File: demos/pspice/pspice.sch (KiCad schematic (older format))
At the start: 20 parts, among them Q1 Q2N2222, Q2 Q2N2222, Q3 Q2N2222

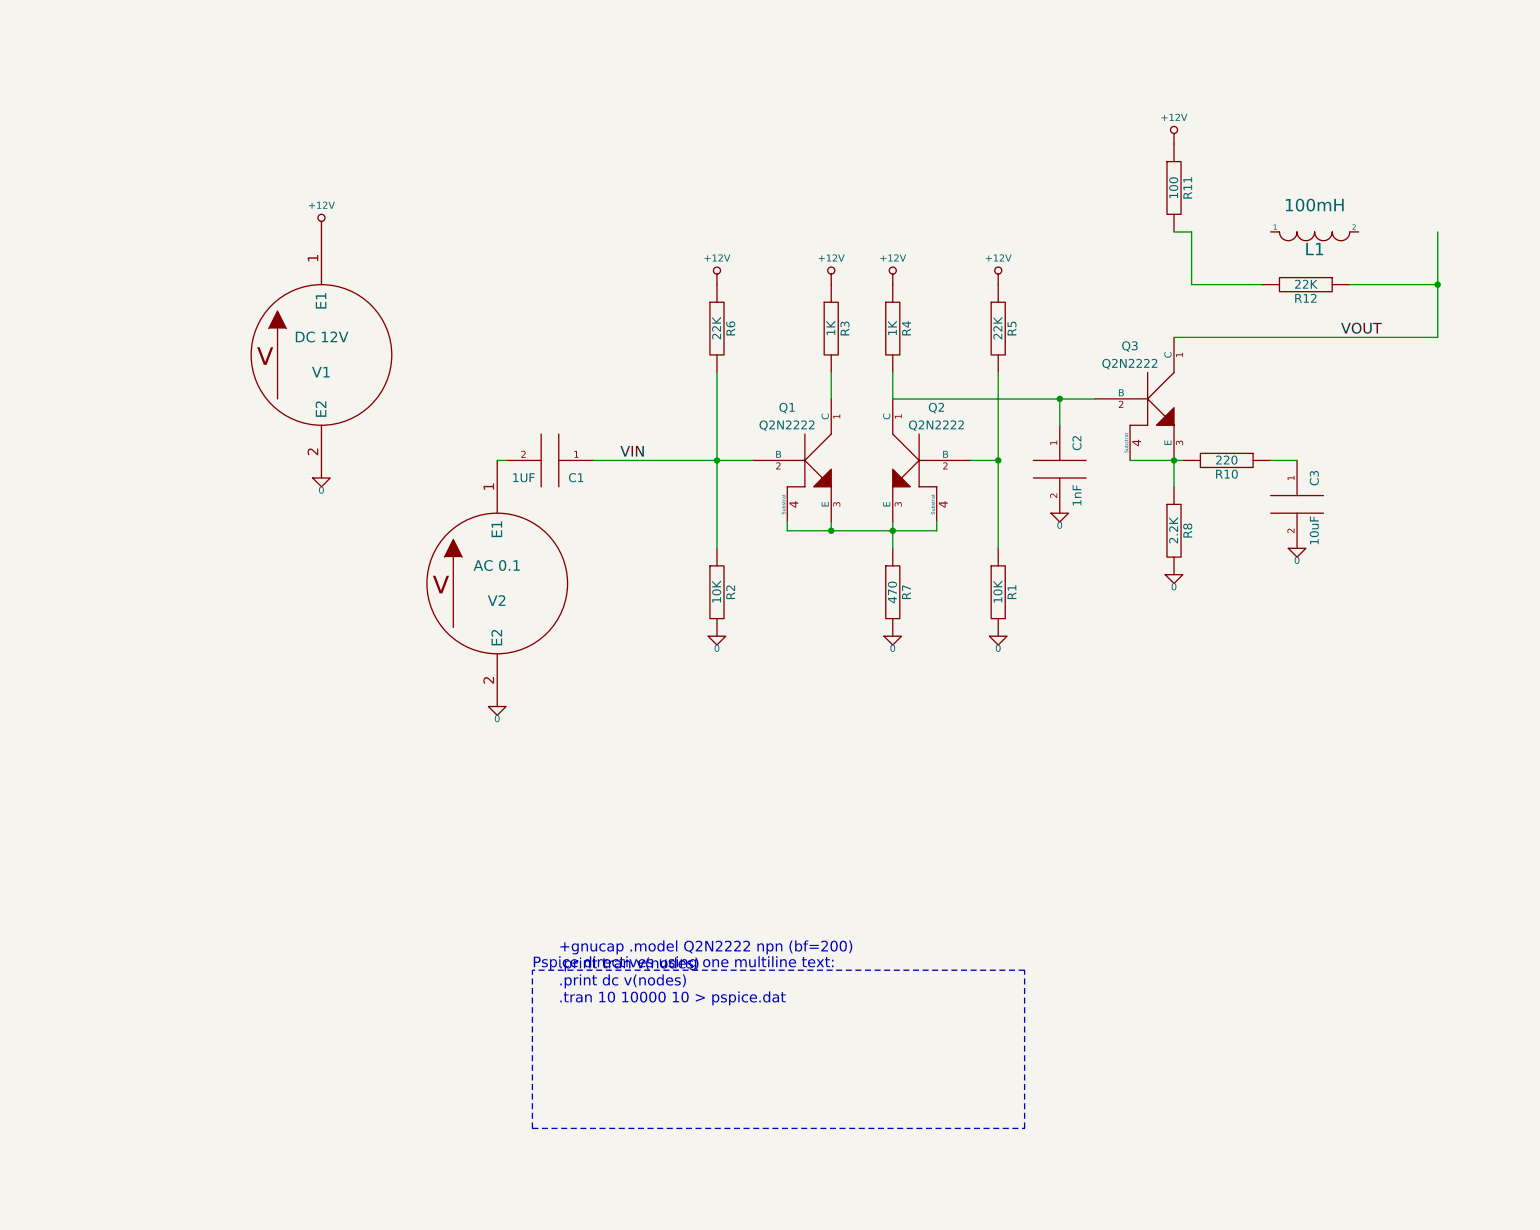
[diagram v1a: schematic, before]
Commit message: Update demos. Fix  pspice netlist issues when using ( and ) in net names ( parenthesis are replaced by underscore) .
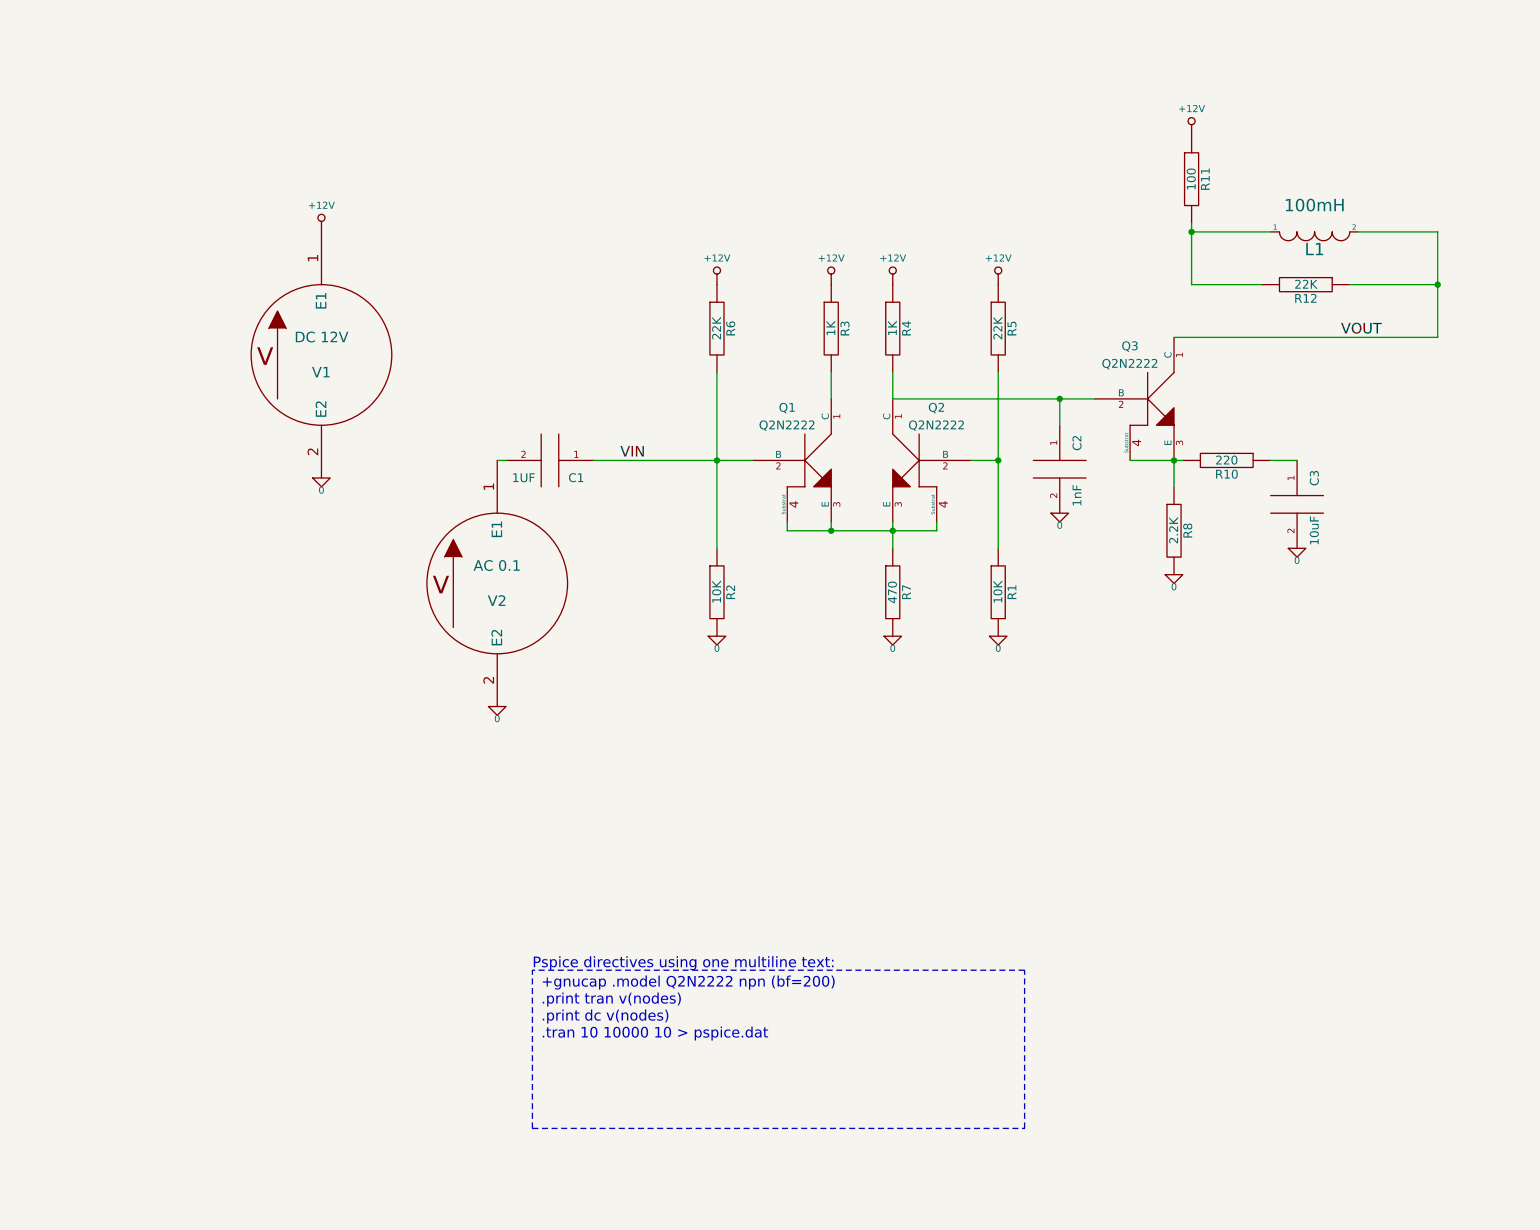
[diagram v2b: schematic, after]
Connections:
- wire segments 23 -> 24
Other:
- moved on the sheet: R11
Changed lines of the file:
@@
-EESchema Schematic File Version 2  date 14/07/2010 20:10:02
+EESchema Schematic File Version 2
 LIBS:pspice
 LIBS:pspice-cache
-EELAYER 24  0
+EELAYER 24 0
 EELAYER END
-$Descr A4 11700 8267
+$Descr A4 11693 8268
+encoding utf-8
 Sheet 1 1
 Title ""
@@
 	6850 5700 4050 5700
 Wire Wire Line
-	5300 2800 4400 2800
+	4400 2800 5300 2800
 Connection ~ 9200 1800
 Wire Wire Line
 	8700 1800 9200 1800
 Wire Wire Line
-	8200 1800 7800 1800
-Wire Wire Line
-	7800 1800 7800 1500
-Wire Wire Line
-	7800 1500 7700 1500
+	7800 1800 8200 1800
+Wire Wire Line
+	7800 1450 7800 1800
+Wire Wire Line
+	7800 1500 8250 1500
 Wire Wire Line
 	9200 1500 9200 2100
@@
 	8250 2800 8400 2800
 Wire Wire Line
-	7750 2800 7450 2800
+	7450 2800 7750 2800
 Connection ~ 7050 2450
 Wire Wire Line
@@
 Connection ~ 6100 3200
 Wire Wire Line
-	6350 3150 6350 3200
-Wire Wire Line
-	6350 3200 5500 3200
+	6350 3200 6350 3150
+Wire Wire Line
+	5500 3200 6350 3200
 Wire Wire Line
 	5750 3150 5750 3200
@@
 	7700 2950 7700 2800
 Wire Wire Line
-	7250 2450 6100 2450
+	6100 2450 7250 2450
 Wire Wire Line
 	6100 2450 6100 2300
@@
 	6700 2300 6700 3300
 Wire Wire Line
-	6100 3300 6100 3150
+	6100 3150 6100 3300
 Wire Wire Line
 	5100 2300 5100 3300
 Wire Wire Line
 	9200 2100 7700 2100
-Text Notes 4200 5900 0    60   ~ 0
+Text Notes 4100 6100 0    60   ~ 0
 +gnucap .model Q2N2222 npn (bf=200)\n.print tran v(nodes)\n.print dc v(nodes)\n.tran 10 10000 10 > pspice.dat\n
 Text Notes 4050 5700 0    60   ~ 0
@@
 F 0 "R12" V 8530 1800 50  0000 C CNN
 F 1 "22K" V 8450 1800 50  0000 C CNN
+F 2 "" H 8450 1800 60  0001 C CNN
+F 3 "" H 8450 1800 60  0001 C CNN
 	1    8450 1800
 	0    1    1    0
@@
 L R R11
 U 1 1 3E9D4D47
-P 7700 1250
-F 0 "R11" V 7780 1250 50  0000 C CNN
-F 1 "100" V 7700 1250 50  0000 C CNN
-	1    7700 1250
+P 7800 1200
+F 0 "R11" V 7880 1200 50  0000 C CNN
+F 1 "100" V 7800 1200 50  0000 C CNN
+F 2 "" H 7800 1200 60  0001 C CNN
+F 3 "" H 7800 1200 60  0001 C CNN
+	1    7800 1200
 	1    0    0    -1
 $EndComp
@@
 F 0 "L1" H 8500 1600 70  0000 C CNN
 F 1 "100mH" H 8500 1350 70  0000 C CNN
+F 2 "" H 8500 1500 60  0001 C CNN
+F 3 "" H 8500 1500 60  0001 C CNN
 	1    8500 1500
 	1    0    0    1
@@
 F 0 "R10" V 8080 2800 50  0000 C CNN
 F 1 "220" V 8000 2800 50  0000 C CNN
+F 2 "" H 8000 2800 60  0001 C CNN
+F 3 "" H 8000 2800 60  0001 C CNN
 	1    8000 2800
 	0    1    1    0
 $EndComp
 $Comp
-L 0 #GND8
+L 0 #GND01
 U 1 1 3E9D3DE2
 P 8400 3300
-F 0 "#GND8" H 8400 3200 40  0001 C CNN
+F 0 "#GND01" H 8400 3200 40  0001 C CNN
 F 1 "0" H 8400 3230 40  0000 C CNN
+F 2 "" H 8400 3300 60  0001 C CNN
+F 3 "" H 8400 3300 60  0001 C CNN
 	1    8400 3300
 	1    0    0    -1
@@
 F 0 "C3" V 8500 3200 50  0000 C CNN
 F 1 "10uF" V 8500 2900 50  0000 C CNN
+F 2 "" H 8400 3050 60  0000 C CNN
+F 3 "" H 8400 3050 60  0000 C CNN
 	1    8400 3050
 	1    0    0    -1
 $EndComp
 $Comp
-L 0 #GND7
+L 0 #GND02
 U 1 1 3E9D1EFF
 P 7050 3100
-F 0 "#GND7" H 7050 3000 40  0001 C CNN
+F 0 "#GND02" H 7050 3000 40  0001 C CNN
 F 1 "0" H 7050 3030 40  0000 C CNN
+F 2 "" H 7050 3100 60  0001 C CNN
+F 3 "" H 7050 3100 60  0001 C CNN
 	1    7050 3100
 	1    0    0    -1
@@
 F 0 "C2" V 7150 3000 50  0000 C CNN
 F 1 "1nF" V 7150 2700 50  0000 C CNN
+F 2 "" H 7050 2850 60  0001 C CNN
+F 3 "" H 7050 2850 60  0001 C CNN
 	1    7050 2850
 	1    0    0    -1
 $EndComp
 $Comp
-L 0 #GND6
+L 0 #GND03
 U 1 1 32E8B852
 P 7700 3450
-F 0 "#GND6" H 7700 3350 40  0001 C CNN
+F 0 "#GND03" H 7700 3350 40  0001 C CNN
 F 1 "0" H 7700 3380 40  0000 C CNN
+F 2 "" H 7700 3450 60  0001 C CNN
+F 3 "" H 7700 3450 60  0001 C CNN
 	1    7700 3450
 	1    0    0    -1
@@
 L +12V #+12V6
 U 1 1 32E8B84A
-P 7700 1000
-F 0 "#+12V6" H 7700 1200 40  0001 C CNN
-F 1 "+12V" H 7700 1150 40  0000 C CNN
-	1    7700 1000
+P 7800 950
+F 0 "#+12V6" H 7800 1150 40  0001 C CNN
+F 1 "+12V" H 7800 1100 40  0000 C CNN
+F 2 "" H 7800 950 60  0001 C CNN
+F 3 "" H 7800 950 60  0001 C CNN
+	1    7800 950
 	1    0    0    -1
 $EndComp
@@
 F 0 "R8" V 7780 3200 50  0000 C CNN
 F 1 "2.2K" V 7700 3200 50  0000 C CNN
+F 2 "" H 7700 3200 60  0001 C CNN
+F 3 "" H 7700 3200 60  0001 C CNN
 	1    7700 3200
 	1    0    0    -1
@@
 F 0 "Q3" H 7450 2750 50  0000 C CNN
 F 1 "Q2N2222" H 7450 2650 50  0000 C CNN
+F 2 "" H 7550 2450 60  0001 C CNN
+F 3 "" H 7550 2450 60  0001 C CNN
 	1    7550 2450
 	1    0    0    -1
 $EndComp
 $Comp
-L 0 #GND5
+L 0 #GND04
 U 1 1 32CFC469
 P 3850 4200
-F 0 "#GND5" H 3850 4100 40  0001 C CNN
+F 0 "#GND04" H 3850 4100 40  0001 C CNN
 F 1 "0" H 3850 4130 40  0000 C CNN
+F 2 "" H 3850 4200 60  0001 C CNN
+F 3 "" H 3850 4200 60  0001 C CNN
 	1    3850 4200
 	1    0    0    -1
@@
 F 0 "V2" H 3850 3400 60  0000 C CNN
 F 1 "AC 0.1" H 3850 3600 60  0000 C CNN
+F 2 "" H 3850 3500 60  0001 C CNN
+F 3 "" H 3850 3500 60  0001 C CNN
 	1    3850 3500
 	1    0    0    -1
@@
 F 0 "C1" V 4250 2950 50  0000 C CNN
 F 1 "1UF" V 4250 2650 50  0000 C CNN
+F 2 "" H 4150 2800 60  0001 C CNN
+F 3 "" H 4150 2800 60  0001 C CNN
 	1    4150 2800
 	0    1    1    0
@@
 F 0 "#+12V5" H 2850 1700 40  0001 C CNN
 F 1 "+12V" H 2850 1650 40  0000 C CNN
+F 2 "" H 2850 1500 60  0001 C CNN
+F 3 "" H 2850 1500 60  0001 C CNN
 	1    2850 1500
 	1    0    0    -1
 $EndComp
 $Comp
-L 0 #GND4
+L 0 #GND05
 U 1 1 32CFC344
 P 2850 2900
-F 0 "#GND4" H 2850 2800 40  0001 C CNN
+F 0 "#GND05" H 2850 2800 40  0001 C CNN
 F 1 "0" H 2850 2830 40  0000 C CNN
+F 2 "" H 2850 2900 60  0001 C CNN
+F 3 "" H 2850 2900 60  0001 C CNN
 	1    2850 2900
 	1    0    0    -1
@@
 F 0 "V1" H 2850 2100 60  0000 C CNN
 F 1 "DC 12V" H 2850 2300 60  0000 C CNN
+F 2 "" H 2850 2200 60  0001 C CNN
+F 3 "" H 2850 2200 60  0001 C CNN
 	1    2850 2200
 	1    0    0    -1
@@
 F 0 "#+12V4" H 6700 2000 40  0001 C CNN
 F 1 "+12V" H 6700 1950 40  0000 C CNN
+F 2 "" H 6700 1800 60  0001 C CNN
+F 3 "" H 6700 1800 60  0001 C CNN
 	1    6700 1800
 	1    0    0    -1
@@
 F 0 "#+12V3" H 6100 2000 40  0001 C CNN
 F 1 "+12V" H 6100 1950 40  0000 C CNN
+F 2 "" H 6100 1800 60  0001 C CNN
+F 3 "" H 6100 1800 60  0001 C CNN
 	1    6100 1800
 	1    0    0    -1
@@
 F 0 "#+12V2" H 5750 2000 40  0001 C CNN
 F 1 "+12V" H 5750 1950 40  0000 C CNN
+F 2 "" H 5750 1800 60  0001 C CNN
+F 3 "" H 5750 1800 60  0001 C CNN
 	1    5750 1800
 	1    0    0    -1
@@
 F 0 "#+12V1" H 5100 2000 40  0001 C CNN
 F 1 "+12V" H 5100 1950 40  0000 C CNN
+F 2 "" H 5100 1800 60  0001 C CNN
+F 3 "" H 5100 1800 60  0001 C CNN
 	1    5100 1800
 	1    0    0    -1
 $EndComp
 $Comp
-L 0 #GND3
+L 0 #GND06
 U 1 1 32CFC2B8
 P 6700 3800
-F 0 "#GND3" H 6700 3700 40  0001 C CNN
+F 0 "#GND06" H 6700 3700 40  0001 C CNN
 F 1 "0" H 6700 3730 40  0000 C CNN
+F 2 "" H 6700 3800 60  0001 C CNN
+F 3 "" H 6700 3800 60  0001 C CNN
 	1    6700 3800
 	1    0    0    -1
 $EndComp
 $Comp
-L 0 #GND2
+L 0 #GND07
 U 1 1 32CFC2B5
 P 5100 3800
-F 0 "#GND2" H 5100 3700 40  0001 C CNN
+F 0 "#GND07" H 5100 3700 40  0001 C CNN
 F 1 "0" H 5100 3730 40  0000 C CNN
+F 2 "" H 5100 3800 60  0001 C CNN
+F 3 "" H 5100 3800 60  0001 C CNN
 	1    5100 3800
 	1    0    0    -1
@@
 F 0 "R2" V 5180 3550 50  0000 C CNN
 F 1 "10K" V 5100 3550 50  0000 C CNN
+F 2 "" H 5100 3550 60  0001 C CNN
+F 3 "" H 5100 3550 60  0001 C CNN
 	1    5100 3550
 	1    0    0    -1
@@
 F 0 "R6" V 5180 2050 50  0000 C CNN
 F 1 "22K" V 5100 2050 50  0000 C CNN
+F 2 "" H 5100 2050 60  0001 C CNN
+F 3 "" H 5100 2050 60  0001 C CNN
 	1    5100 2050
 	1    0    0    -1
@@
 F 0 "R5" V 6780 2050 50  0000 C CNN
 F 1 "22K" V 6700 2050 50  0000 C CNN
+F 2 "" H 6700 2050 60  0001 C CNN
+F 3 "" H 6700 2050 60  0001 C CNN
 	1    6700 2050
 	1    0    0    -1
@@
 F 0 "R1" V 6780 3550 50  0000 C CNN
 F 1 "10K" V 6700 3550 50  0000 C CNN
+F 2 "" H 6700 3550 60  0001 C CNN
+F 3 "" H 6700 3550 60  0001 C CNN
 	1    6700 3550
 	1    0    0    -1
 $EndComp
 $Comp
-L 0 #GND1
+L 0 #GND08
 U 1 1 32CFC26C
 P 6100 3800
-F 0 "#GND1" H 6100 3700 40  0001 C CNN
+F 0 "#GND08" H 6100 3700 40  0001 C CNN
 F 1 "0" H 6100 3730 40  0000 C CNN
+F 2 "" H 6100 3800 60  0001 C CNN
+F 3 "" H 6100 3800 60  0001 C CNN
 	1    6100 3800
 	1    0    0    -1
@@
 F 0 "R7" V 6180 3550 50  0000 C CNN
 F 1 "470" V 6100 3550 50  0000 C CNN
+F 2 "" H 6100 3550 60  0001 C CNN
+F 3 "" H 6100 3550 60  0001 C CNN
 	1    6100 3550
 	1    0    0    -1
@@
 F 0 "R4" V 6180 2050 50  0000 C CNN
 F 1 "1K" V 6100 2050 50  0000 C CNN
+F 2 "" H 6100 2050 60  0001 C CNN
+F 3 "" H 6100 2050 60  0001 C CNN
 	1    6100 2050
 	1    0    0    -1
@@
 F 0 "R3" V 5830 2050 50  0000 C CNN
 F 1 "1K" V 5750 2050 50  0000 C CNN
+F 2 "" H 5750 2050 60  0001 C CNN
+F 3 "" H 5750 2050 60  0001 C CNN
 	1    5750 2050
 	1    0    0    -1
@@
 F 0 "Q2" H 6150 3100 50  0000 C CNN
 F 1 "Q2N2222" H 6150 3000 50  0000 C CNN
+F 2 "" H 6250 2800 60  0001 C CNN
+F 3 "" H 6250 2800 60  0001 C CNN
 	1    6250 2800
 	-1   0    0    -1
@@
 F 0 "Q1" H 5500 3100 50  0000 C CNN
 F 1 "Q2N2222" H 5500 3000 50  0000 C CNN
+F 2 "" H 5600 2800 60  0001 C CNN
+F 3 "" H 5600 2800 60  0001 C CNN
 	1    5600 2800
 	1    0    0    -1
 $EndComp
+Wire Wire Line
+	9200 1500 8750 1500
+Connection ~ 7800 1500
 $EndSCHEMATC

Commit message: demos/ schematic tidying
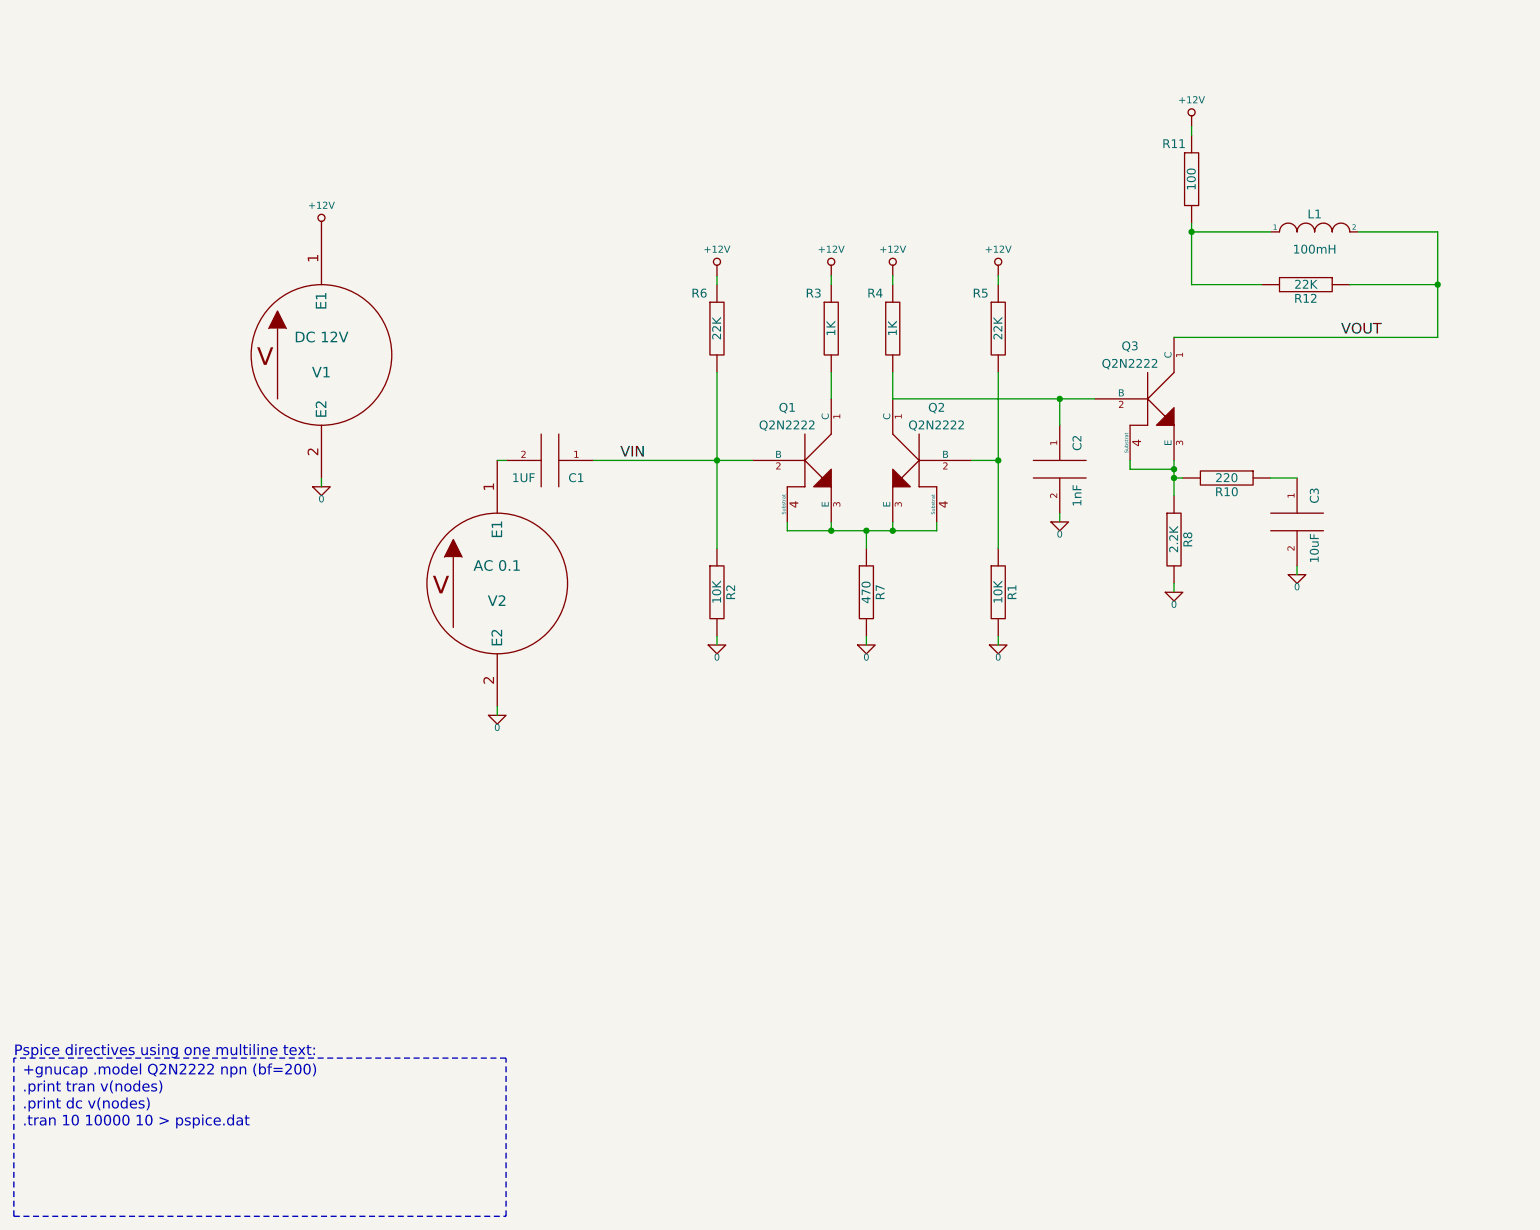
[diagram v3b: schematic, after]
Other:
- moved on the sheet: C3, L1, R10, R7, R8

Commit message: merge from production git:c0bb8a3 31.05.2017
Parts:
- removed R10: 220, symbol R
- added C4: 10nF, symbol CAP
- added L2: 100mH, symbol INDUCTOR
- added R12: 100, symbol R
- added R7: 22K, symbol R
- C2: value 1nF -> 220pF
- C3: value 10uF -> 10nF
- R1: renamed from R11; value 100 -> 10
- V1: value DC 12V -> DC 12
- V2: value AC 0.1 -> AC; Spice_Model (none) -> dc 0 ac 1; Spice_Netlist_Enabled (none) -> Y; Spice_Primitive (none) -> V
- renumbered Q3 to Q1, Q1 to Q2, Q2 to Q3, R7 to R10, R1 to R11, R12 to R2, R6 to R3, R3 to R4, R4 to R5, R5 to R6, R2 to R9
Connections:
- net labels added: VBASE
- wire segments 40 -> 50
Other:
- note added: ".model Q2N2222 npn (bf=200)\n.ac dec 100 10 1Meg\n"
- note removed: "+gnucap .model Q2N2222 npn (bf=200)\n.print tran v(nodes)\n.print dc v(nodes)\n.tran 10 10000 10 > pspice.dat\n"
- moved on the sheet: C3
